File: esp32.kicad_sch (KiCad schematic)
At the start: 52 parts, among them J2 Conn_01x05, SW1 Reset, SW2 BOOT, U15 MPR121QR2, U8 ESP32-S3R8, U9 W25Q128JVSIQ, Y1 40MHz

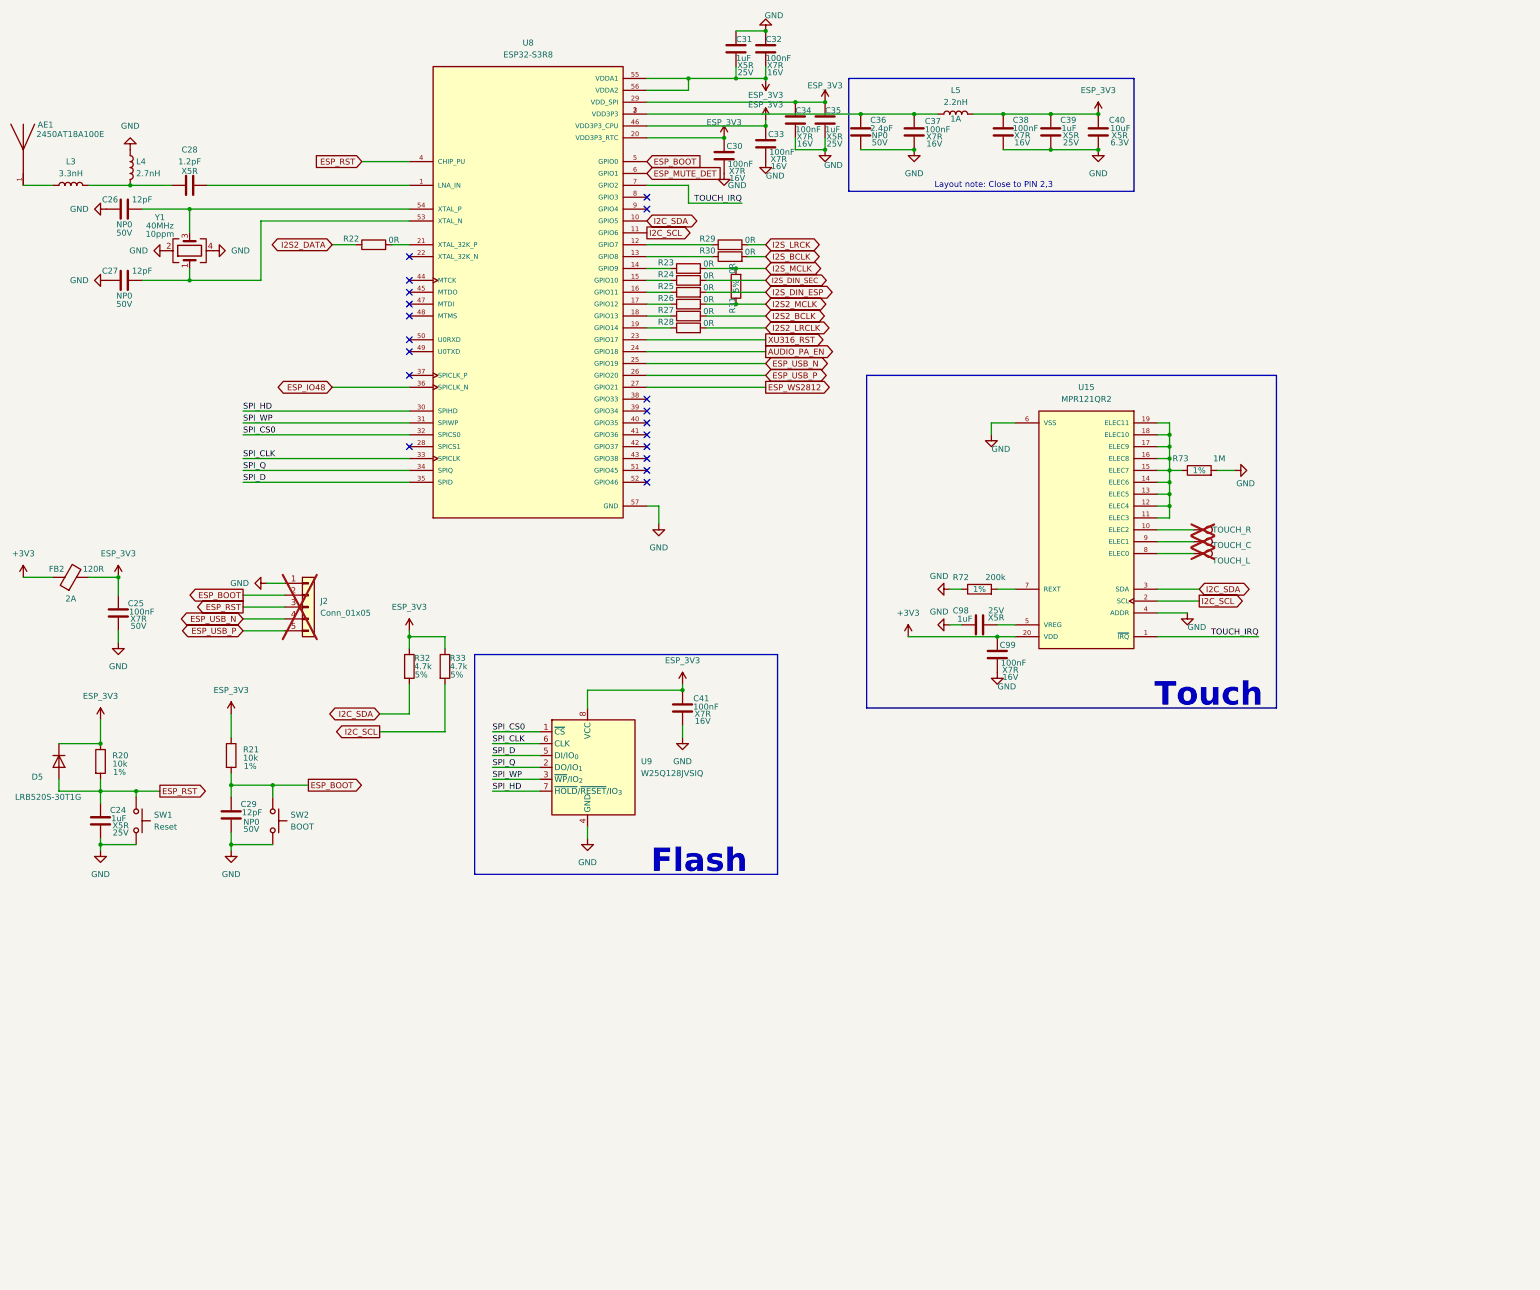
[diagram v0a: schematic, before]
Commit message: adding esp32c6 for OTBR
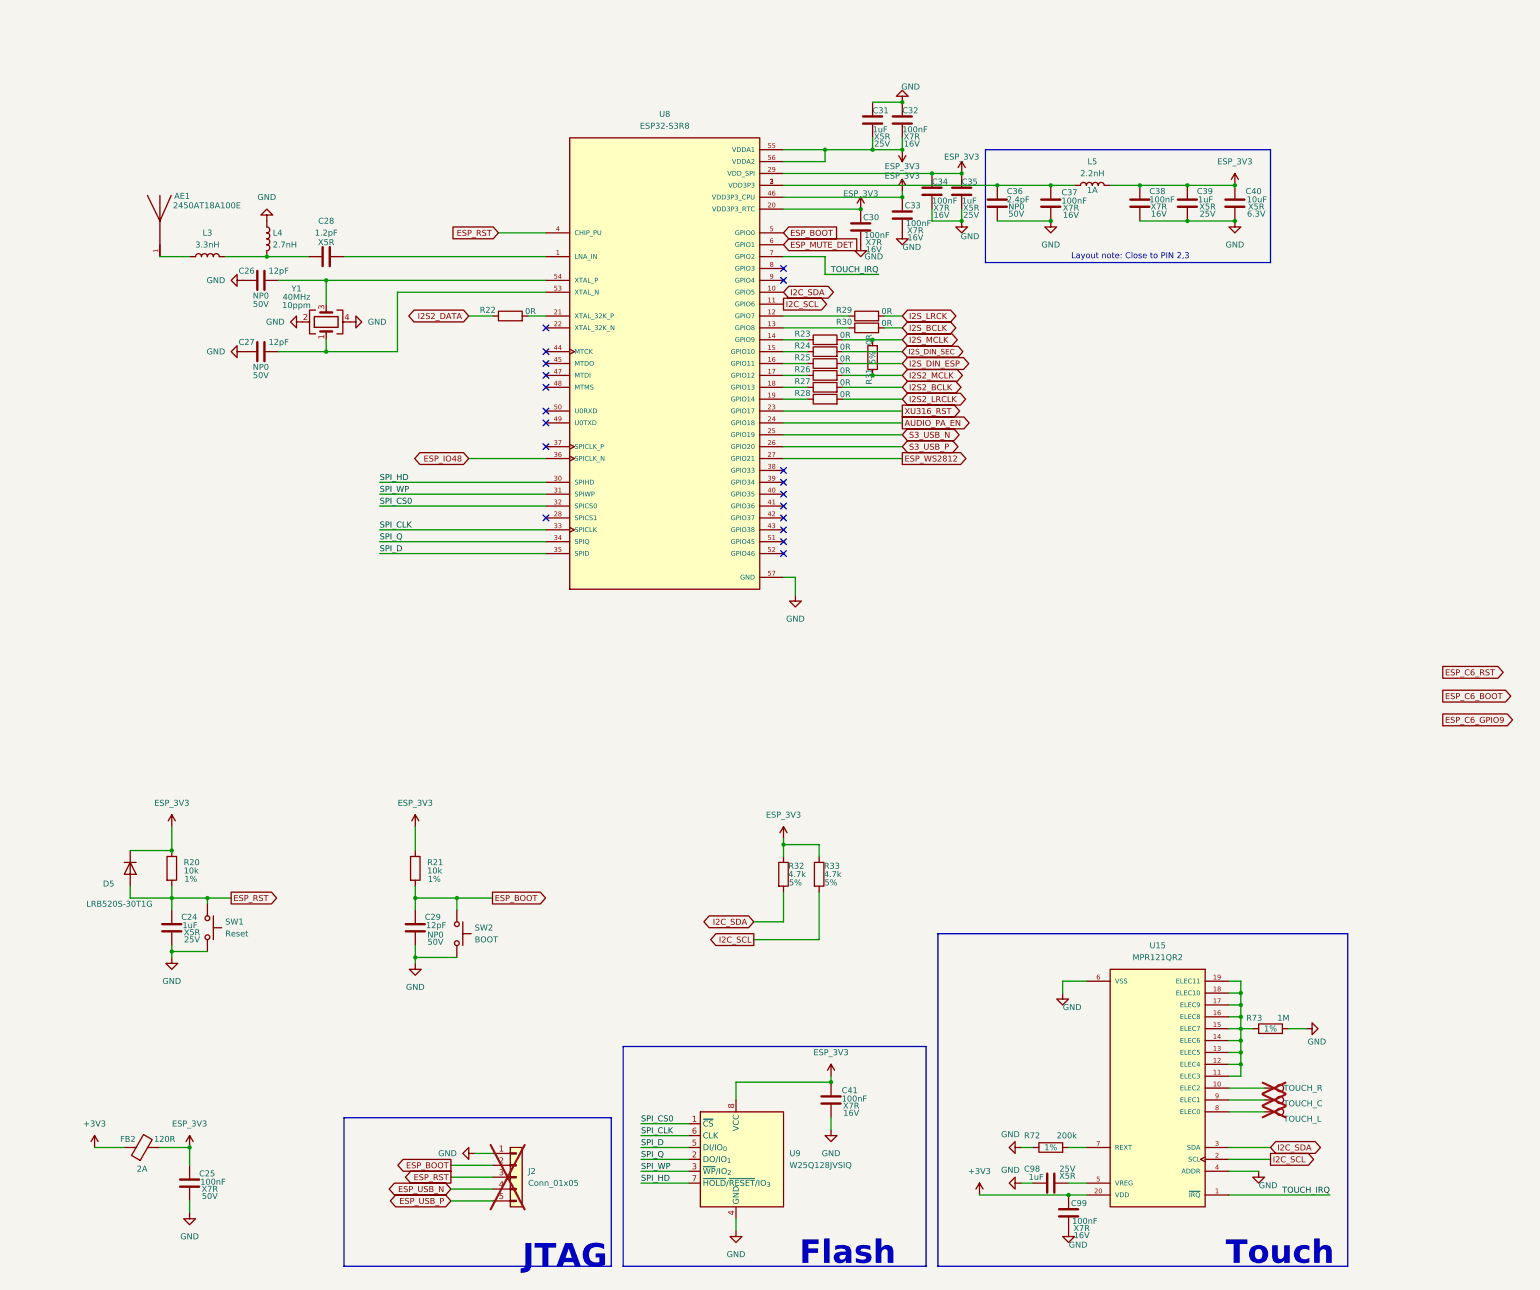
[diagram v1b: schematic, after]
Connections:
- net ESP_USB_N: no longer U8.25 (GPIO19)
- net ESP_USB_P: no longer U8.26 (GPIO20)
- new net S3_USB_N: U8.25 (GPIO19)
- new net S3_USB_P: U8.26 (GPIO20)
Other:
- note added: "JTAG"
- moved on the sheet: AE1, C24, C25, C26, C27, C28, C29, C30, C31, C32, C33, C34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

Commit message: WiP update
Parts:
- TP14, TP15, TP16: footprint TestPoint:TestPoint_Pad_2.5x2.5mm -> Onju:Touchpad
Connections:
- net ESP_USB_N is gone; now on net S3_USB_N: J2.4 (Pin_4)
- net ESP_USB_P is gone; now on net S3_USB_P: J2.5 (Pin_5)
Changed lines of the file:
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@@
 		)
 	)
-	(global_label "ESP_USB_N"
+	(global_label "S3_USB_N"
 		(shape bidirectional)
 		(at 106.68 264.16 180)
@@
 		)
 		(property "Intersheetrefs" "${INTERSHEET_REFS}"
-			(at 91.8793 264.16 0)
+			(at 93.0888 264.16 0)
 			(effects
 				(font
@@
 		)
 	)
-	(global_label "ESP_USB_P"
+	(global_label "S3_USB_P"
 		(shape bidirectional)
 		(at 106.68 266.7 180)
@@
 		)
 		(property "Intersheetrefs" "${INTERSHEET_REFS}"
-			(at 91.9398 266.7 0)
+			(at 93.1493 266.7 0)
 			(effects
 				(font
@@
 			)
 		)
-		(property "Footprint" "TestPoint:TestPoint_Pad_2.5x2.5mm"
+		(property "Footprint" "Onju:Touchpad"
 			(at 280.67 250.19 0)
 			(effects
@@
 			)
 		)
-		(property "Footprint" "TestPoint:TestPoint_Pad_2.5x2.5mm"
+		(property "Footprint" "Onju:Touchpad"
 			(at 280.67 247.65 0)
 			(effects
@@
 			)
 		)
-		(property "Footprint" "TestPoint:TestPoint_Pad_2.5x2.5mm"
+		(property "Footprint" "Onju:Touchpad"
 			(at 280.67 252.73 0)
 			(effects

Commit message: Publish KiCad 10 hardware updates
Refresh the Nest Mini v2 drop-in PCB project in KiCad 10 and publish the accumulated schematic and board updates as a single clean mainline change.

Remove the unused USB-C power/input branch from the power sheet, including the USB connector path, data switching, VBUS switching, and associated support parts, while preserving the pogo-accessible USB signals where needed. Add the ESP32-C6 1x05 pogo connector with the J2-style pin order for GND, boot, reset, USB D-, and USB D+ without a 3.3 V pin.

Add a 5 V SN74AHCT1G125 buffer for the LED data input, with local decoupling and a 47 ohm series output resistor, so the LED chain receives a buffered LED_WS2812_5V signal from the ESP_WS2812 control net.

Carry forward the KiCad 10 project save state and schematic cleanups for the XMOS, ESP32, audio, LED, and power sheets without changing the TAS amplifier topology.
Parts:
- renumbered C24 to C20, C25 to C21, C26 to C22, C27 to C23, C28 to C24, C29 to C25, C41 to C26, C30 to C27, C31 to C28, C32 to C29, C33 to C30, C34 to C31, C35 to C32, C36 to C33, C37 to C34, C98 to C35, C99 to C36, C38 to C37, C39 to C38, C40 to C39, D5 to D1, FB2 to FB1, J2 to J1, L3 to L4, L4 to L5, L5 to L6, R20 to R15, R21 to R16, R22 to R17, R32 to R18, R33 to R19, R23 to R20, R24 to R21, R25 to R22, R26 to R23, R27 to R24, R28 to R25, R29 to R26, R30 to R27, R31 to R28, R72 to R29, R73 to R30, TP14 to TP5, TP15 to TP6, TP16 to TP7, U8 to U5, U9 to U6, U15 to U7
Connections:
- net ESP_C6_GPIO9: now also U5.44 (MTCK)
- net ESP_C6_RST: now also U5.43 (GPIO38)
- net C6_UA0RXD: now reaches U5.37 (SPICLK_P)
- net ESP_IO48 renamed C6_UA0TXD
- no-connect marks 19 -> 16

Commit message: Publish ESP32-P4 multi-sheet hardware redesign
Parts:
- removed SW1: Reset, Onju:SW-SMD_4P-L4.2-W3.2-P2.15-LS4.5, symbol Switch:SW_Push
- removed SW2: BOOT, Onju:SW-SMD_4P-L4.2-W3.2-P2.15-LS4.5, symbol Switch:SW_Push
- AE1, C20, C21, C22, C23, C24, C25, C26, C27, C28, C29, C30, C31, C32, C33, C34, C37, C38, C39, D1, FB1, L4, L5, L6, R15, R16, R18, R19, R28, U5, U6, Y1: Function ESP32 -> ESP32-S3
- C35, C36, R29, R30: Function ESP32 -> TOUCH
- J1, R17, R20, R21: Function (none) -> ESP32-S3
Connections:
- net ESP_BOOT: no longer C25.1, R16.2, U5.5 (GPIO0)
- net ESP_RST: no longer C20.1, D1.2 (A), R15.2, U5.4 (CHIP_PU)
- net at TP6.1: now also U7.8 (ELEC0); no longer U7.9 (ELEC1)
- net at TP7.1: now also U7.9 (ELEC1); no longer U7.8 (ELEC0)
- new net S3_BOOT: C25.1, R16.2, U5.5 (GPIO0)
- new net S3_RST: C20.1, D1.2 (A), R15.2, U5.4 (CHIP_PU)

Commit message: Update KiCad schematics and PCB layout
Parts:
- removed R17, R20, R21, R22, R23, R24, R25, R26, R27, R28: 0R, Resistor_SMD:R_0402_1005Metric, symbol Device:R
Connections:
- net ESP_BOOT is gone; now on net S3_BOOT: J1.2 (Pin_2)
- net ESP_RST is gone; now on net S3_RST: J1.3 (Pin_3)
- net I2S2_BCLK: now also U5.18 (GPIO13)
- net I2S2_LRCLK: now also U5.19 (GPIO14)
- net I2S2_MCLK: now also U5.17 (GPIO12)
- net I2S_BCLK: now also U5.13 (GPIO8)
- net I2S_DIN_ESP: now also U5.16 (GPIO11)
- net I2S_DIN_SEC: now also U5.15 (GPIO10)
- net I2S_LRCK: now also U5.12 (GPIO7)
- net I2S_MCLK: now also U5.14 (GPIO9)
- net XU316_RST: no longer names the net of U5.23 (GPIO17)
- no-connect marks 16 -> 18
